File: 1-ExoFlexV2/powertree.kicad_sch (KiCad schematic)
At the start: 55 parts, among them J5 Jumper, J6 Jumper, J7 Jumper 5,2A, J71 Jumper 5,2A, J8 USB-C, J81 14 AWG, U123 LDO -5VA, U124 LDO 5VA, U14 TVS 24V, U5 DCDC24V/8V, U6 DCDC24V/5V NUM, U7 DCDC 24V/-7,8V ANA

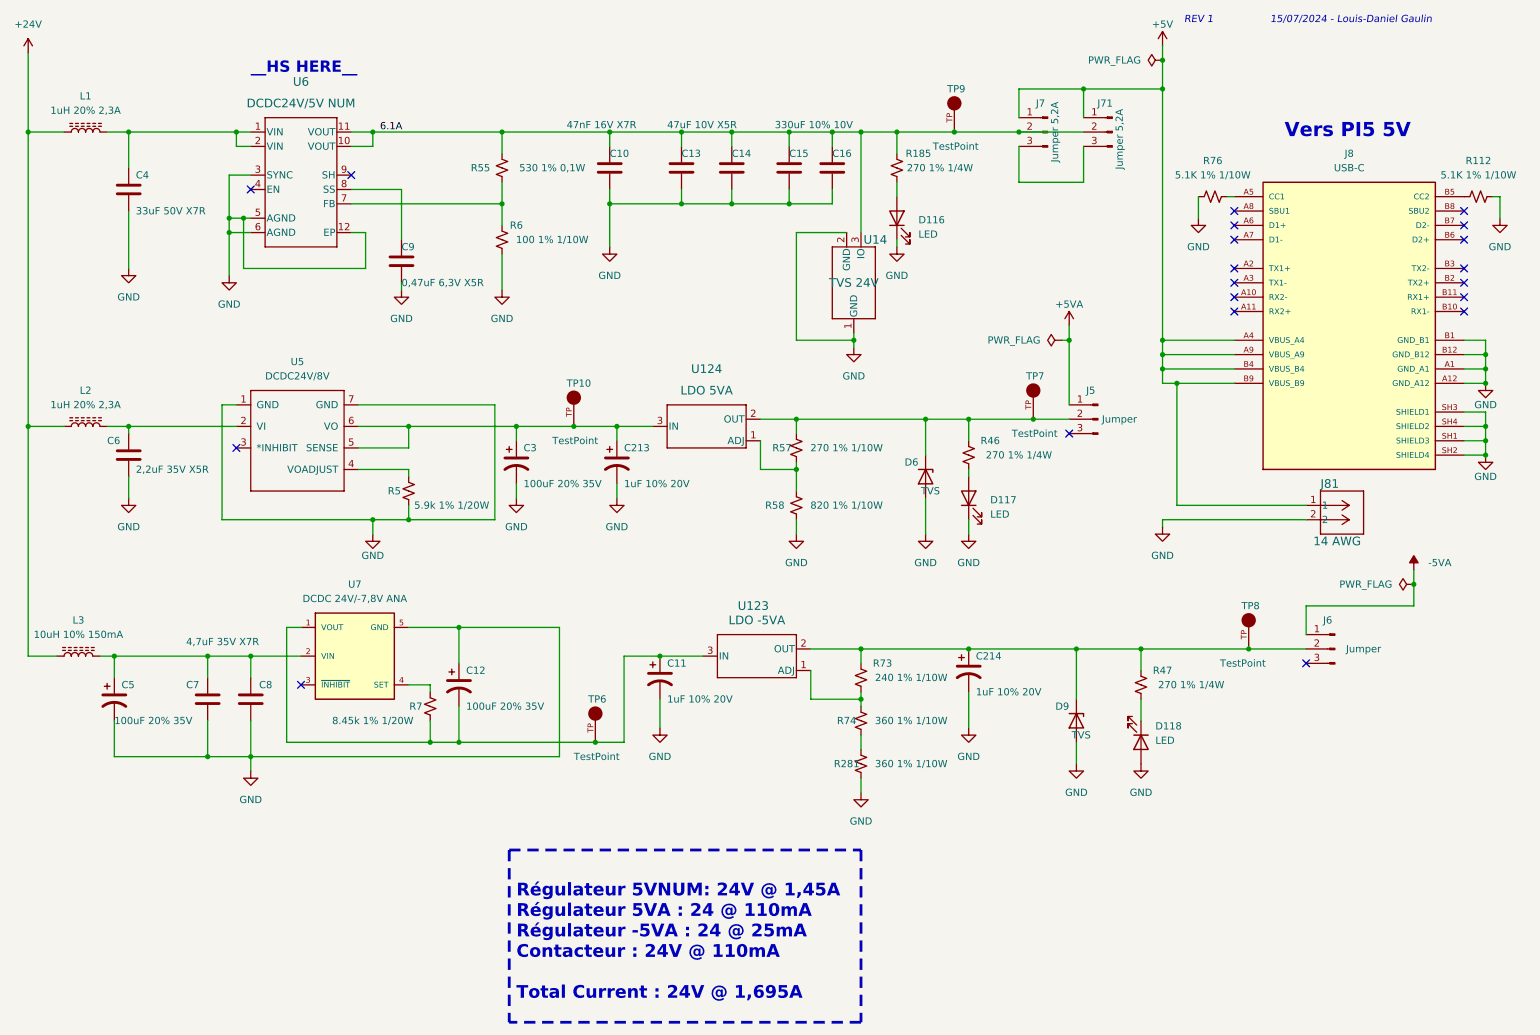
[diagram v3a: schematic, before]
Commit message: Layout Review 1
- Routing fone Alimentation et ADC
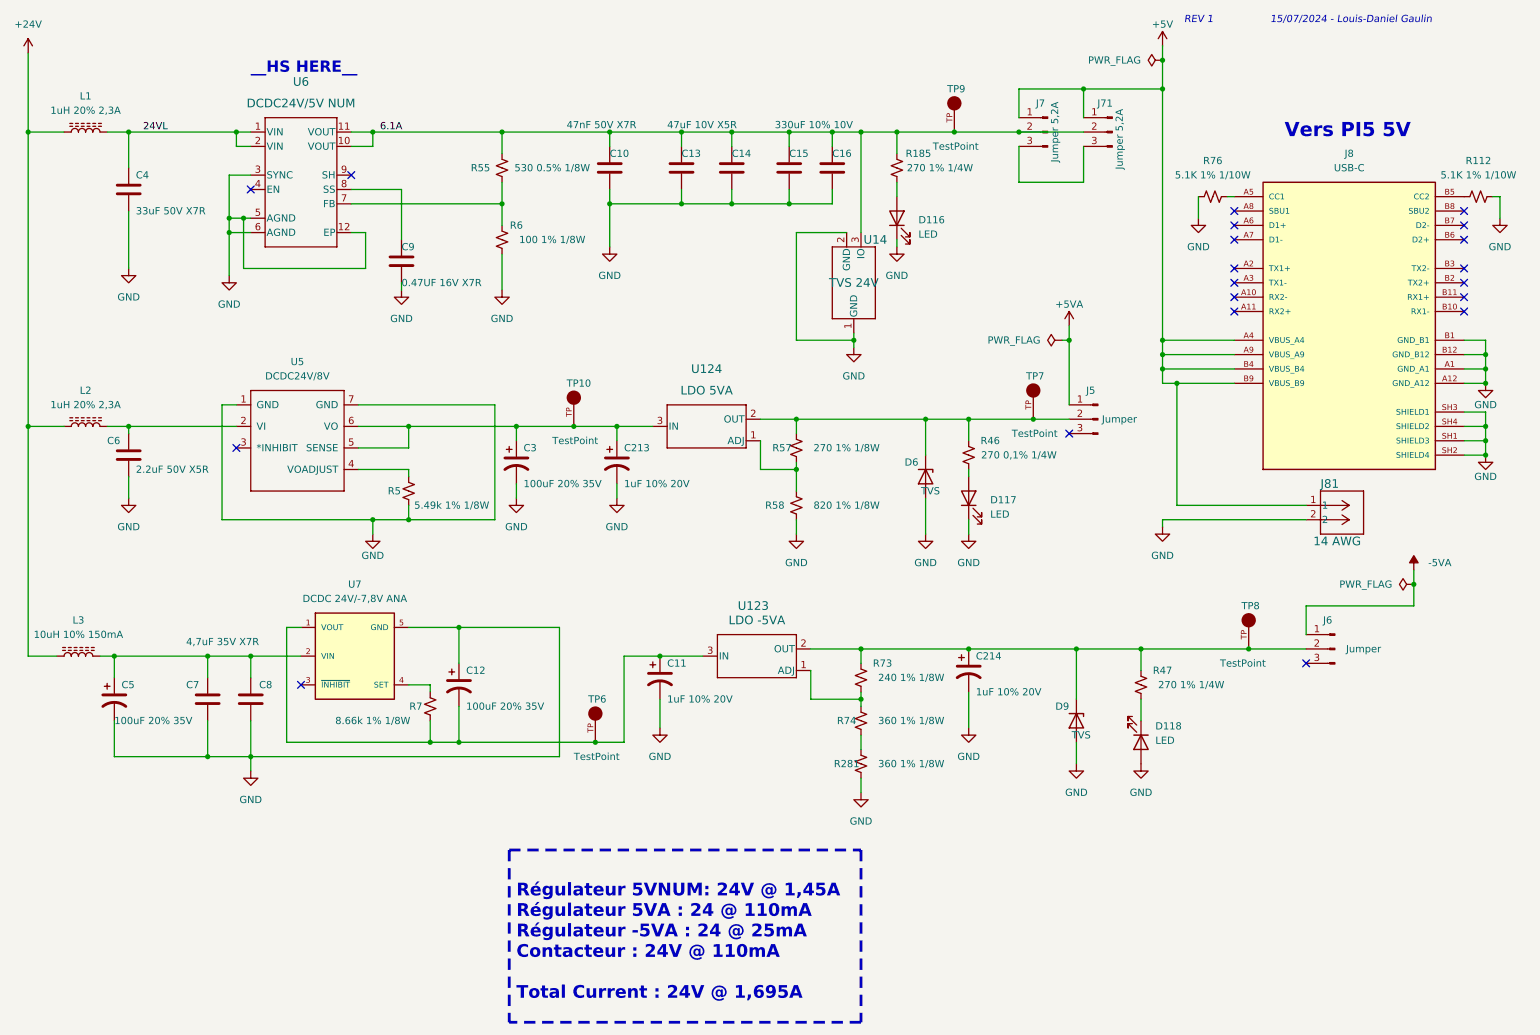
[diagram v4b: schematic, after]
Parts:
- C10: value 47nF 16V X7R -> 47nF 50V X7R; footprint Capacitor_SMD:C_0603_1608Metric -> Capacitor_SMD:C_1206_3216Metric; DESCRIPTION 0.047 µF ±20% 16V Ceramic Capacitor X7R 0603 (1608 Metric) -> 0.047 µF ±10% 50V Ceramic Capacitor X7R 1206 (3216 Metric); MANUFACTURER Johanson Dielectrics Inc. -> YAGEO; PACKAGE 0603 (1608 Metric -> 1206 (3216 Metric); PART NUMBER EMCP160W473M1GV001T -> CC1206KRX7R9BB473
- C6: value 2,2uF 35V X5R -> 2.2uF 50V X5R; footprint Capacitor_SMD:C_0603_1608Metric -> Capacitor_SMD:C_0805_2012Metric; DESCRIPTION 2.2 µF ±10% 35V Ceramic Capacitor X5R 0603 (1608 Metric) -> 2.2 µF ±10% 50V Ceramic Capacitor X5R 0805 (2012 Metric); PACKAGE 0603 (1608 Metric) -> 0805 (2012 Metric); PART NUMBER GRM188R6YA225KA12D -> GRT21BR61H225KE13L
- C9: value 0,47uF 6,3V X5R -> 0.47UF 16V X7R; footprint Capacitor_SMD:C_01005_0402Metric -> Capacitor_SMD:C_0805_2012Metric; DESCRIPTION 0.47 µF ±20% 6.3V Ceramic Capacitor X5R 01005 (0402 Metric) -> 0.47 µF ±10% 16V Ceramic Capacitor X7R 0805 (2012 Metric); MANUFACTURER Murata Electronics -> KYOCERA AVX; PACKAGE 01005 (0402 Metric) -> 0805 (2012 Metric); PART NUMBER GRM022R60J474ME15L -> KGM21AR71C474KU
- R281, R74: value 360 1% 1/10W -> 360 1% 1/8W; footprint Resistor_SMD:R_0603_1608Metric -> Resistor_SMD:R_0805_2012Metric; DESCRIPTION 360 Ohms ±1% 0.1W, 1/10W Chip Resistor 0603 (1608 Metric) A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 -> 360 Ohms ±1% 0.125W, 1/8W Chip Resistor 0805 (2012 Metric) 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; PACKAGE 0603 (1608 Metric) -> 0805 (2012 Metric); PART NUMBER ERJ-3EKF3600V -> ERJ-6ENF3600V
- R46: value 270 1% 1/4W -> 270 0,1% 1/4W
- R5: value 5.9k 1% 1/20W -> 5.49k 1% 1/8W; footprint Resistor_SMD:R_0201_0603Metric -> Resistor_SMD:R_0805_2012Metric; DESCRIPTION 5.9 kOhms ±1% 0.05W, 1/20W Chip Resistor 0201 (0603 Metric)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 -> 5.49 kOhms ±1% 0.125W, 1/8W Chip Resistor 0805 (2012 Metric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; MANUFACTURER Panasonic Electronic Components -> YAGEO; PACKAGE 0201 (0603 Metric) -> 0805 (2012 Metric); PART NUMBER ERJ-1GNF5901C -> RC0805FR-075K49L
- R55: value 530 1% 0,1W -> 530 0.5% 1/8W; footprint Resistor_SMD:R_0603_1608Metric -> Resistor_SMD:R_0805_2012Metric; DESCRIPTION 530 Ohms ±1% 0.1W, 1/10W Chip Resistor 0603 (1608 Metric) A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 -> 530 Ohms ±0.5% 0.125W, 1/8W Chip Resistor 0805 (2012 Metric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; PACKAGE 0603 (1608 Metric) -> 0805 (2012 Metric); PART NUMBER RN73H1JTTD5300F25 -> RN73R2ATTD5300D25
- R57: value 270 1% 1/10W -> 270 1% 1/8W; footprint Resistor_SMD:R_0603_1608Metric -> Resistor_SMD:R_0805_2012Metric; DESCRIPTION 270 Ohms ±1% 0.1W, 1/10W Chip Resistor 0603 (1608 Metric) A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 -> 270 Ohms ±1% 0.125W, 1/8W Chip Resistor 0805 (2012 Metric) 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; PACKAGE 0603 (1608 Metric) -> 0805 (2012 Metric); PART NUMBER ERJ-3EKF2700V -> ERJ-6ENF2700V
- R58: value 820 1% 1/10W -> 820 1% 1/8W; footprint Resistor_SMD:R_0603_1608Metric -> Resistor_SMD:R_0805_2012Metric; DESCRIPTION RES SMD 820 OHM 1% 1/10W 0603 -> 820 Ohms ±1% 0.125W, 1/8W Chip Resistor 0805 (2012 Metric) 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; PACKAGE 0603 (1608 Metric) -> 0805 (2012 Metric); PART NUMBER ERJ-3EKF8200V -> ERJ-6ENF8200V
- R6: value 100 1% 1/10W -> 100 1% 1/8W; footprint Resistor_SMD:R_0603_1608Metric -> Resistor_SMD:R_0805_2012Metric; DESCRIPTION 100 Ohms ±1% 0.1W, 1/10W Chip Resistor 0603 (1608 Metric) A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 -> 100 Ohms ±1% 0.125W, 1/8W Chip Resistor 0805 (2012 Metric) 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; PACKAGE 0603 (1608 Metric) -> 0805 (2012 Metric); PART NUMBER ERJ-3EKF1000V -> ERJ-6ENF1000V
- R7: value 8.45k 1% 1/20W -> 8.66k 1% 1/8W; footprint Resistor_SMD:R_0201_0603Metric -> Resistor_SMD:R_0805_2012Metric; DESCRIPTION 8.45 kOhms ±1% 0.05W, 1/20W Chip Resistor 0201 (0603 Metric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 -> 8.66 kOhms ±1% 0.125W, 1/8W Chip Resistor 0805 (2012 Metric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; PACKAGE 0201 (0603 Metric) -> 0805 (2012 Metric); PART NUMBER ERJ-1GNF8451C -> ERJ-6ENF8661V
- R73: value 240 1% 1/10W -> 240 1% 1/8W; footprint Resistor_SMD:R_0603_1608Metric -> Resistor_SMD:R_0805_2012Metric; DESCRIPTION 240 Ohms ±1% 0.1W, 1/10W Chip Resistor 0603 (1608 Metric) A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 -> 240 Ohms ±1% 0.125W, 1/8W Chip Resistor 0805 (2012 Metric) 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; PACKAGE 0603 (1608 Metric) -> 0805 (2012 Metric); PART NUMBER ERJ-3EKF2400V -> ERJ-6ENF2400V
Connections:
- net 24VL: now reaches C4.1, L1.2, U6.1 (VIN), U6.2 (VIN)

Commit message: Final
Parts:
- U123: footprint FootPrintLib:TO92260P482H934-3N -> FootPrintLib:T03B_TEX
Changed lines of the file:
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@@
       (effects (font (size 1.27 1.27) italic) hide)
     )
-    (property "Datasheet" "" (id 3) (at 138.43 96.52 0)
+    (property "Datasheet" "LM338T/NOPB" (id 3) (at 138.43 96.52 0)
       (effects (font (size 1.27 1.27) italic) hide)
     )
@@
     (pin "1")
   )
-  (symbol (lib_id "SymLib:LM338T_NOPB") (at 118.11 128.27 0) (unit 1)
+  (symbol (lib_name "LM338T_NOPB_1") (lib_id "SymLib:LM338T_NOPB") (at 118.11 128.27 0) (unit 1)
     (in_bom yes) (on_board yes)
     (property "Reference" "U123" (id 0) (at 146.05 120.65 0)
@@
       (effects (font (size 1.524 1.524)))
     )
-    (property "Footprint" "FootPrintLib:TO92260P482H934-3N" (id 2) (at 147.32 137.16 0)
+    (property "Footprint" "FootPrintLib:T03B_TEX" (id 2) (at 147.32 137.16 0)
       (effects (font (size 1.27 1.27) italic) hide)
     )
-    (property "Datasheet" "" (id 3) (at 147.32 137.16 0)
+    (property "Datasheet" "LM338T/NOPB" (id 3) (at 147.32 137.16 0)
       (effects (font (size 1.27 1.27) italic) hide)
     )

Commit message: LAst changes
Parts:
- U123: footprint FootPrintLib:T03B_TEX -> FootPrintLib:TO92260P482H934-3N
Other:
- note added: "Régulateur 5VNUM: 24V @ 1,45A Régulateur 5VA : 24V @ 110mA Régulateur -5VA : 24V @ 25mA Contacteur : 24V @ 110mA Total Current : 24V @ 1,695A"
- note removed: "Régulateur 5VNUM: 24V @ 1,45A Régulateur 5VA : 24 @ 110mA Régulateur -5VA : 24 @ 25mA Contacteur : 24V @ 110mA Total Current : 24V @ 1,695A"
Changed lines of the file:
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@@
     (effects (font (size 2.5 2.5) (thickness 0.5) bold) (justify left bottom))
   )
-  (text "Régulateur 5VNUM: 24V @ 1,45A\nRégulateur 5VA : 24 @ 110mA\nRégulateur -5VA : 24 @ 25mA\nContacteur : 24V @ 110mA\n\nTotal Current : 24V @ 1,695A"
+  (text "Régulateur 5VNUM: 24V @ 1,45A\nRégulateur 5VA : 24V @ 110mA\nRégulateur -5VA : 24V @ 25mA\nContacteur : 24V @ 110mA\n\nTotal Current : 24V @ 1,695A"
     (at 104.14 190.5 0)
     (effects (font (size 2.25 2.25) (thickness 0.45) bold) (justify left bottom))
@@
       (effects (font (size 1.524 1.524)))
     )
-    (property "Footprint" "FootPrintLib:T03B_TEX" (id 2) (at 147.32 137.16 0)
+    (property "Footprint" "FootPrintLib:TO92260P482H934-3N" (id 2) (at 147.32 137.16 0)
       (effects (font (size 1.27 1.27) italic) hide)
     )

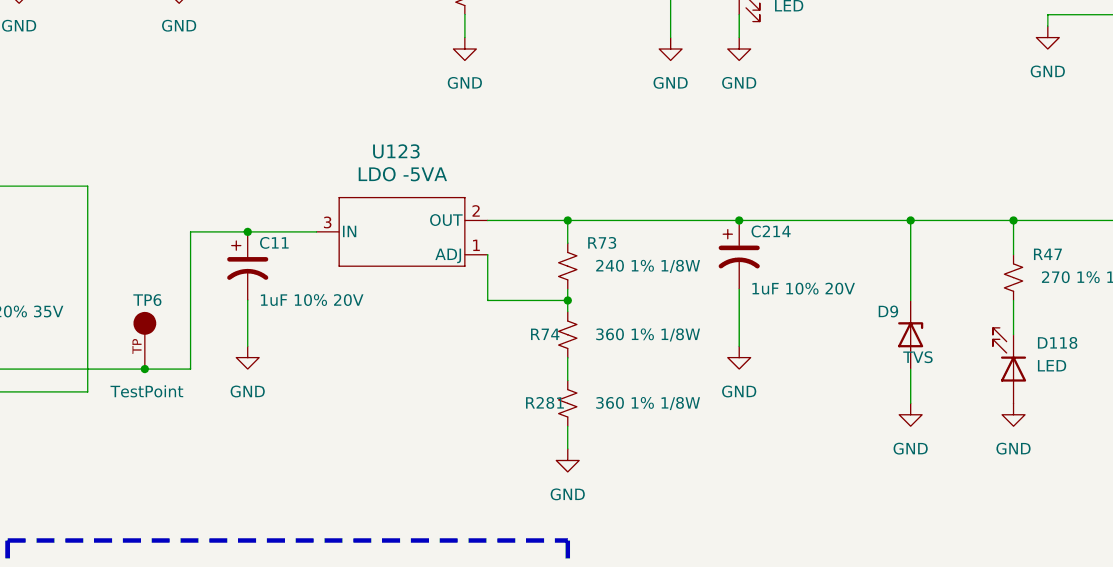
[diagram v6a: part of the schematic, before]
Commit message: Analyse Post-PMC
-Modification du footprint du régulateur de tension
- Inversion des condos et diode sur les tensions négative
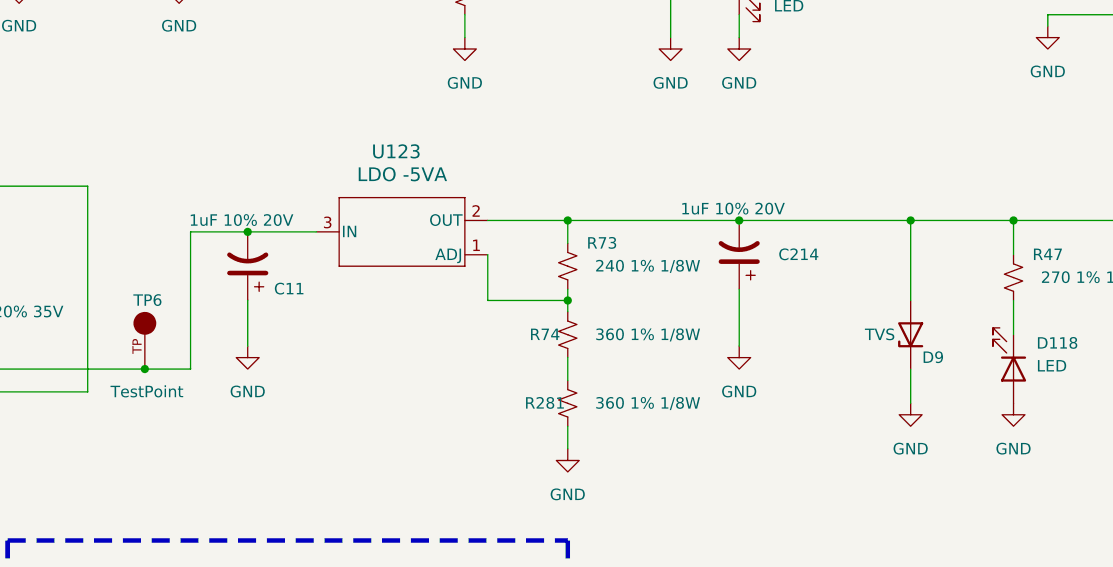
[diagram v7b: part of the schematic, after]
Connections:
- net GND: now also C11.1, C214.1, D9.1 (K); no longer C11.2, C214.2, D9.2 (A)
- net at J6.2 (Pin_2), R47.2, R73.2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: now also C214.2, D9.2 (A); no longer C214.1, D9.1 (K)
- net at C12.2, R7.1, TP6.TP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: now also C11.2; no longer C11.1
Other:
- moved on the sheet: C11, C214, D9
